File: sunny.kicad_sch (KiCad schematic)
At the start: 53 parts, among them J2 Screw_Terminal_01x03, Q1 FQPF7N90C, T1 7508112339, U10 Optocoupler_DC_PhotoNPN_AKEC, U11 TL431D, U4 MIC4684, U5 UC3842N, U9 AP2112K-3.3, X2 B2P-VH

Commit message: Initialtes
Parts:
- added D5: D_Zener, Diode_THT:D_5KP_P12.70mm_Horizontal, symbol Device:D_Zener
- U5: footprint UC3842N:DIP794W45P254L959H508Q8 -> kaam25_footprints_symbol:DIP794W45P254L959H508Q8
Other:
- moved on the sheet: R_startUp1, R_startUp2, R_startUp3
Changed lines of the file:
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@@
 	)
 	(junction
-		(at 148.59 38.1)
+		(at 186.69 102.87)
 		(diameter 0)
 		(color 0 0 0 0)
 	)
 	(junction
-		(at 186.69 102.87)
+		(at 76.2 81.28)
 		(diameter 0)
 		(color 0 0 0 0)
 	)
 	(junction
-		(at 76.2 81.28)
+		(at 148.59 99.06)
 		(diameter 0)
 		(color 0 0 0 0)
@@
 	)
 	(junction
-		(at 148.59 99.06)
+		(at 148.59 38.1)
 		(diameter 0)
 		(color 0 0 0 0)
@@
 	(wire
 		(pts
-			(xy 148.59 96.52) (xy 148.59 99.06)
+			(xy 148.59 71.12) (xy 148.59 99.06)
 		)
 		(stroke
@@
 	(wire
 		(pts
-			(xy 148.59 85.09) (xy 148.59 88.9)
+			(xy 148.59 59.69) (xy 148.59 63.5)
 		)
 		(stroke
@@
 	(wire
 		(pts
-			(xy 148.59 38.1) (xy 148.59 66.04)
+			(xy 148.59 38.1) (xy 148.59 40.64)
 		)
 		(stroke
@@
 	(wire
 		(pts
-			(xy 148.59 73.66) (xy 148.59 77.47)
+			(xy 148.59 48.26) (xy 148.59 52.07)
 		)
 		(stroke
@@
 			)
 		)
-		(property "Footprint" "UC3842N:DIP794W45P254L959H508Q8"
+		(property "Footprint" "kaam25_footprints_symbol:DIP794W45P254L959H508Q8"
 			(at 97.79 137.16 0)
 			(hide yes)
@@
 		(dnp no)
 		(property "Reference" "R_snub1"
-			(at 150.622 53.594 0)
+			(at 160.274 49.022 0)
 			(show_name no)
 			(do_not_autoplace no)
@@
 		)
 		(property "Value" "17"
-			(at 150.622 56.134 0)
+			(at 160.274 51.562 0)
 			(show_name no)
 			(do_not_autoplace no)
@@
 	(symbol
 		(lib_id "Device:R")
-		(at 148.59 92.71 0)
+		(at 148.59 67.31 0)
 		(mirror x)
 		(unit 1)
@@
 		(dnp no)
 		(property "Reference" "R_startUp3"
-			(at 154.94 92.71 90)
+			(at 154.94 67.31 90)
 			(show_name no)
 			(do_not_autoplace no)
@@
 		)
 		(property "Value" "68k"
-			(at 152.4 92.71 90)
+			(at 152.4 67.31 90)
 			(show_name no)
 			(do_not_autoplace no)
@@
 		)
 		(property "Footprint" "Resistor_THT:R_Axial_DIN0309_L9.0mm_D3.2mm_P20.32mm_Horizontal"
-			(at 146.812 92.71 90)
+			(at 146.812 67.31 90)
 			(hide yes)
 			(show_name no)
@@
 		)
 		(property "Datasheet" ""
-			(at 148.59 92.71 0)
+			(at 148.59 67.31 0)
 			(hide yes)
 			(show_name no)
@@
 		)
 		(property "Description" "starup voltage flows through before aux winding start supplying it, HV resistor, 0.5W, 310Volts"
-			(at 148.59 92.71 0)
+			(at 148.59 67.31 0)
 			(hide yes)
 			(show_name no)
@@
 	(symbol
 		(lib_id "Device:R")
-		(at 148.59 81.28 0)
+		(at 148.59 55.88 0)
 		(mirror x)
 		(unit 1)
@@
 		(dnp no)
 		(property "Reference" "R_startUp2"
-			(at 154.94 81.28 90)
+			(at 154.94 55.88 90)
 			(show_name no)
 			(do_not_autoplace no)
@@
 		)
 		(property "Value" "68k"
-			(at 152.4 81.28 90)
+			(at 152.4 55.88 90)
 			(show_name no)
 			(do_not_autoplace no)
@@
 		)
 		(property "Footprint" "Resistor_THT:R_Axial_DIN0309_L9.0mm_D3.2mm_P20.32mm_Horizontal"
-			(at 146.812 81.28 90)
+			(at 146.812 55.88 90)
 			(hide yes)
 			(show_name no)
@@
 		)
 		(property "Datasheet" ""
-			(at 148.59 81.28 0)
+			(at 148.59 55.88 0)
 			(hide yes)
 			(show_name no)
@@
 		)
 		(property "Description" "starup voltage flows through before aux winding start supplying it, HV resistor,0.5W, 310V"
-			(at 148.59 81.28 0)
+			(at 148.59 55.88 0)
 			(hide yes)
 			(show_name no)
@@
 	(symbol
 		(lib_id "Device:R")
-		(at 148.59 69.85 0)
+		(at 148.59 44.45 0)
 		(mirror x)
 		(unit 1)
@@
 		(dnp no)
 		(property "Reference" "R_startUp1"
-			(at 154.94 69.85 90)
+			(at 154.94 44.45 90)
 			(show_name no)
 			(do_not_autoplace no)
@@
 		)
 		(property "Value" "68k"
-			(at 152.4 69.85 90)
+			(at 152.4 44.45 90)
 			(show_name no)
 			(do_not_autoplace no)
@@
 		)
 		(property "Footprint" "Resistor_THT:R_Axial_DIN0309_L9.0mm_D3.2mm_P20.32mm_Horizontal"
-			(at 146.812 69.85 90)
+			(at 146.812 44.45 90)
 			(hide yes)
 			(show_name no)
@@
 		)
 		(property "Datasheet" ""
-			(at 148.59 69.85 0)
+			(at 148.59 44.45 0)
 			(hide yes)
 			(show_name no)
@@
 		)
 		(property "Description" "starup voltage flows through before aux winding start supplying it, HV resistor,0.5W, 310V"
-			(at 148.59 69.85 0)
+			(at 148.59 44.45 0)
 			(hide yes)
 			(show_name no)
@@
 					(unit 1)
 				)
+			)
+		)
+	)
+	(symbol
+		(lib_id "Device:D_Zener")
+		(at 156.21 85.09 270)
+		(unit 1)
+		(body_style 1)
+		(exclude_from_sim no)
+		(in_bom yes)
+		(on_board yes)
+		(in_pos_files yes)
+		(dnp no)
+		(fields_autoplaced yes)
+		(property "Reference" "D5"
+			(at 158.75 83.8199 90)
+			(show_name no)
+			(do_not_autoplace no)
+			(effects
+				(font
+					(size 1.27 1.27)
+				)
+				(justify left)
+			)
+		)
+		(property "Value" "D_Zener"
+			(at 158.75 86.3599 90)
+			(show_name no)
+			(do_not_autoplace no)
+			(effects
+				(font
+					(size 1.27 1.27)
+				)
+				(justify left)
+			)
+		)
+		(property "Footprint" "Diode_THT:D_5KP_P12.70mm_Horizontal"
+			(at 156.21 85.09 0)
+			(hide yes)
+			(show_name no)
+			(do_not_autoplace no)
+			(effects
+				(font
+					(size 1.27 1.27)
+				)
+			)
+		)
+		(property "Datasheet" ""
+			(at 156.21 85.09 0)
+			(hide yes)
+			(show_name no)
+			(do_not_autoplace no)
+			(effects
+				(font
+					(size 1.27 1.27)
+				)
+			)
+		)
+		(property "Description" "Zener diode"
+			(at 156.21 85.09 0)
+			(hide yes)
+			(show_name no)
+			(do_not_autoplace no)
+			(effects
+				(font
+					(size 1.27 1.27)
+				)
+			)
+		)
+		(pin "1"
+		)
+		(pin "2"
+		)
+		(instances
+			(project "chandra_queenofnight"
+				(path "/fe3f1796-d4c1-46ec-bdb5-a29f35c8d4af/43d0d107-b03e-4228-bd2c-42b72694ee16"
+					(reference "D5")
+					(unit 1)
+				)

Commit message: Initialtes 130426
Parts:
- removed D5: D_Zener, Diode_THT:D_5KP_P12.70mm_Horizontal, symbol Device:D_Zener
- removed FL1: Choke_CommonMode_PulseElectronics_PH9455x826NL, Inductor_THT:L_CommonMode_PulseElectronics_PH9455xxx6NL_2, symbol Filter:Choke_CommonMode_PulseElectronics_PH9455x826NL
- R_startUp1, R_startUp2: value 68k -> 83k
- R_startUp3: value 68k -> 1.26k
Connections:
- net GND1: now also R_startUp3.1
- net L: now also D3.4
- net N: now also D3.2
- net VCC: now also R_startUp2.1, R_startUp3.2; no longer R_startUp3.1
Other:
- moved on the sheet: C_filter3, R_startUp3

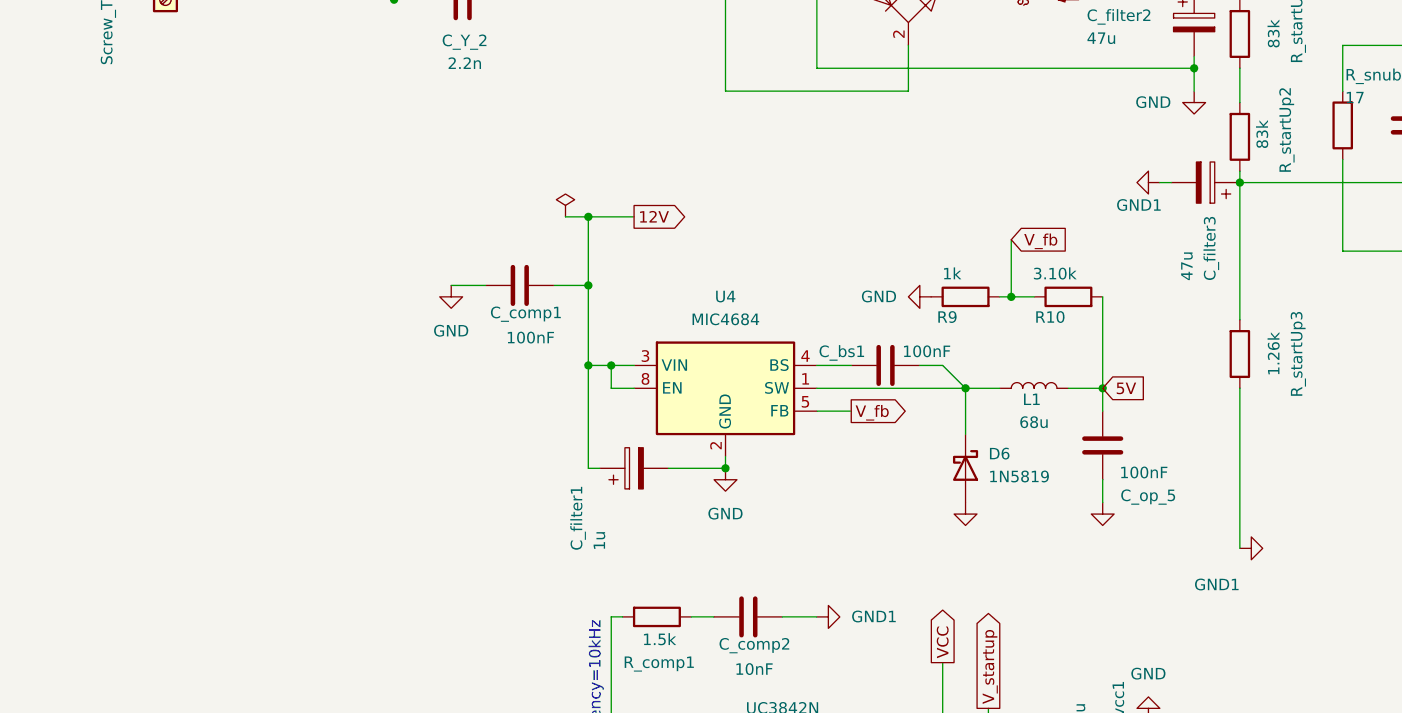
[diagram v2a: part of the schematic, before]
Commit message: Initialtes gndplane
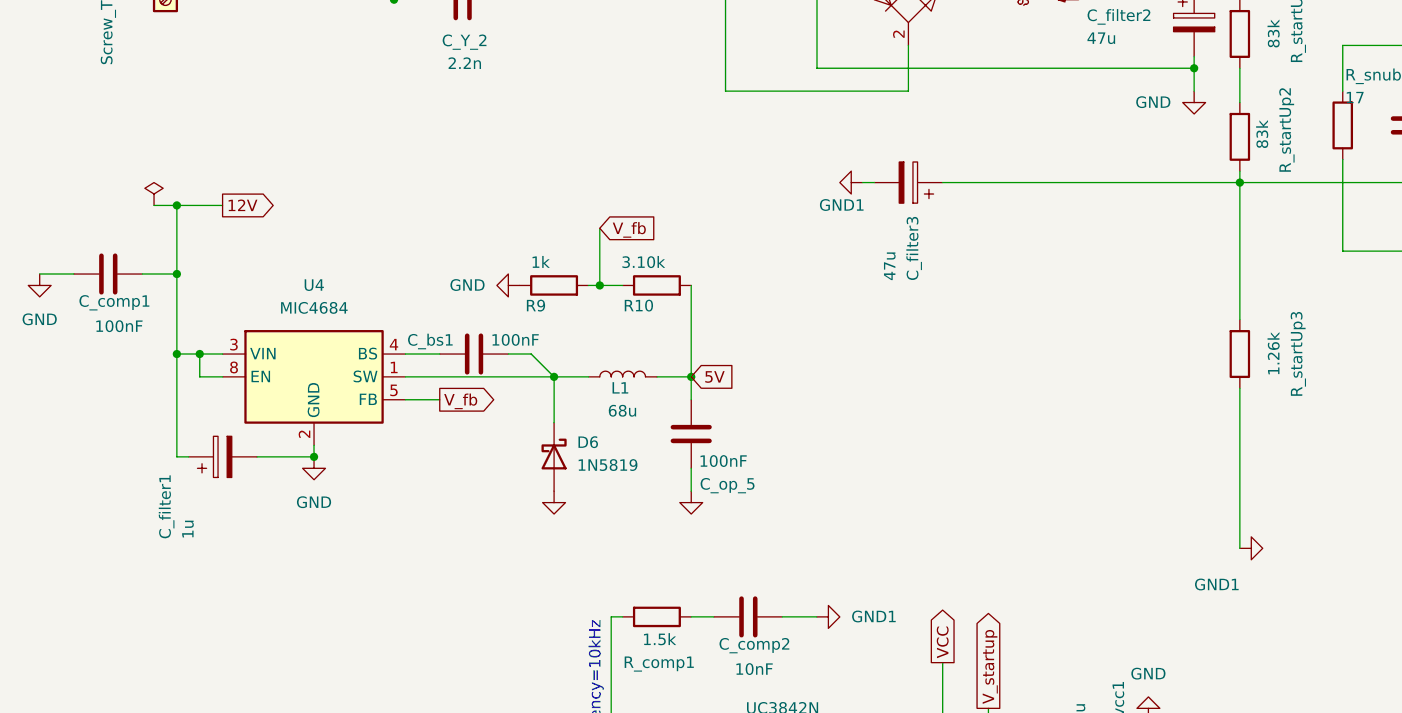
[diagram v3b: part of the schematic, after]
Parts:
- J2: footprint TerminalBlock_MetzConnect:TerminalBlock_MetzConnect_360291_1x01_Horizontal_ScrewM3.0_Boxed -> TerminalBlock_MetzConnect:TerminalBlock_MetzConnect_Type011_RT05503HBLC_1x03_P5.00mm_Horizontal
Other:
- moved on the sheet: C_bs1, C_comp1, C_filter1, C_filter3, C_op_5, D6, L1, R10, R9, U4

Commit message: Initialtes apr21
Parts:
- R_comp1: value 1.5k -> 10k
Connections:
- net GND: now also C_T1.1, C_bypass1.1, C_comp2.1, C_filter3.2, R_Fb1.1, R_sense1.2, R_startUp3.1, U10.3, U5.5 (GND)
- net GND1: no longer C_T1.1, C_bypass1.1, C_comp2.1, C_filter3.2, R_Fb1.1, R_sense1.2, R_startUp3.1, U10.3, U5.5 (GND)

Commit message: Initialtes apr24
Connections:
- net GND: no longer C_comp1.2, C_filter1.2, C_op_5.1, D6.2 (A), R9.1, U4.2 (GND), U4.6 (GND), U4.7 (GND)
- net GND1: now also C_comp1.2, C_filter1.2, C_op_5.1, D6.2 (A), R9.1, U4.2 (GND), U4.6 (GND), U4.7 (GND)

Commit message: Initialtes apr26
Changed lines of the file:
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@@
 	(wire
 		(pts
-			(xy 148.59 83.82) (xy 148.59 101.6)
+			(xy 148.59 83.82) (xy 148.59 91.44)
 		)
 		(stroke
@@
 	(symbol
 		(lib_id "power:GND")
-		(at 148.59 101.6 0)
+		(at 148.59 91.44 0)
 		(unit 1)
 		(body_style 1)
@@
 		(fields_autoplaced yes)
 		(property "Reference" "#PWR038"
-			(at 148.59 107.95 0)
+			(at 148.59 97.79 0)
 			(hide yes)
 			(show_name no)
@@
 		)
 		(property "Value" "GND"
-			(at 148.59 106.68 0)
+			(at 148.59 96.52 0)
 			(show_name no)
 			(do_not_autoplace no)
@@
 		)
 		(property "Footprint" ""
-			(at 148.59 101.6 0)
+			(at 148.59 91.44 0)
 			(hide yes)
 			(show_name no)
@@
 		)
 		(property "Datasheet" ""
-			(at 148.59 101.6 0)
+			(at 148.59 91.44 0)
 			(hide yes)
 			(show_name no)
@@
 		)
 		(property "Description" "Power symbol creates a global label with name \"GND\" , ground"
-			(at 148.59 101.6 0)
+			(at 148.59 91.44 0)
 			(hide yes)
 			(show_name no)

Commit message: Initialtes draft1
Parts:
- C3, C_T1, C_X1, C_Y_1, C_Y_2, C_bp_1, C_bs1, C_bypass1, C_comp1, C_comp2, C_filter1, C_filter2, C_filter3, C_in1, C_op_5, C_out1, C_snub1, C_vcc1: KiLib_Generator (none) -> capacitor/THT/other
- D4, D6, D_fastSwitchig_out1, D_fastSwitchig_out2, D_snub1: KiLib_Generator (none) -> diode/THT
- J2: KiLib_Generator (none) -> terminal_block/Metz_Connect
- L1: KiLib_Generator (none) -> choke_THT
- Q1: KiLib_Generator (none) -> package/TO_SOT/THT
- R10, R9, R_Fb1, R_T1, R_comp1, R_down1, R_gate1, R_led1, R_pullDown1, R_sense1, R_snub1, R_startUp1, R_startUp2, R_startUp3, R_up1, R_vcc1, TH1: KiLib_Generator (none) -> resistor/THT
- U10: KiLib_Generator (none) -> package/DIP/legacy
- U11, U4, U9: KiLib_Generator (none) -> package/gullwing
- X2: KiLib_Generator (none) -> connector/JST
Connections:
- net VCC renamed v_startup
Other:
- moved on the sheet: X2
